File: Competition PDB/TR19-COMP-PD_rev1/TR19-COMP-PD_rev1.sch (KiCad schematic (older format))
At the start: 118 parts, among them J1 PWR BTN, J10 RGB_LED3, J11 Sen1, J12 Sen2, J13 Sen3, J14 Sen4, J15 BTN1, J16 BTN2, J17 BTN3, J18 BTN4, J19 BTN5, J2 PWR_LED, J20 BTN6, J21 BTN7, J22 BTN8, J23 BTN9, J24 Sen5, J25 Sen6, J26 Sen7, J27 Sen8, J28 BTN10, J29 BTN11, J3 PTT_LED, J30 BTN12, J31 BTN13, J32 BTN14, J33 BTN15, J34 BTN16, J35 LED1, J36 LED2, J37 LED3, J38 LED4, J39 LED5, J4 Servo1, J40 LED6, J41 LED7, J42 LED8, J43 LED9, J44 LED10, J45 LED11, J46 LED12, J47 LED13, J48 LED14, J49 LED15, J5 Servo2, J50 LED16, J6 Servo3, J7 BATT CONN, J8 RGB_LED1, J9 RGB_LED2, U1 SN74AHCT125_N_14, U2 SN74AHCT125_N_14, U3 SN74AHCT125_N_14, U4 SN74AHCT125_N_14

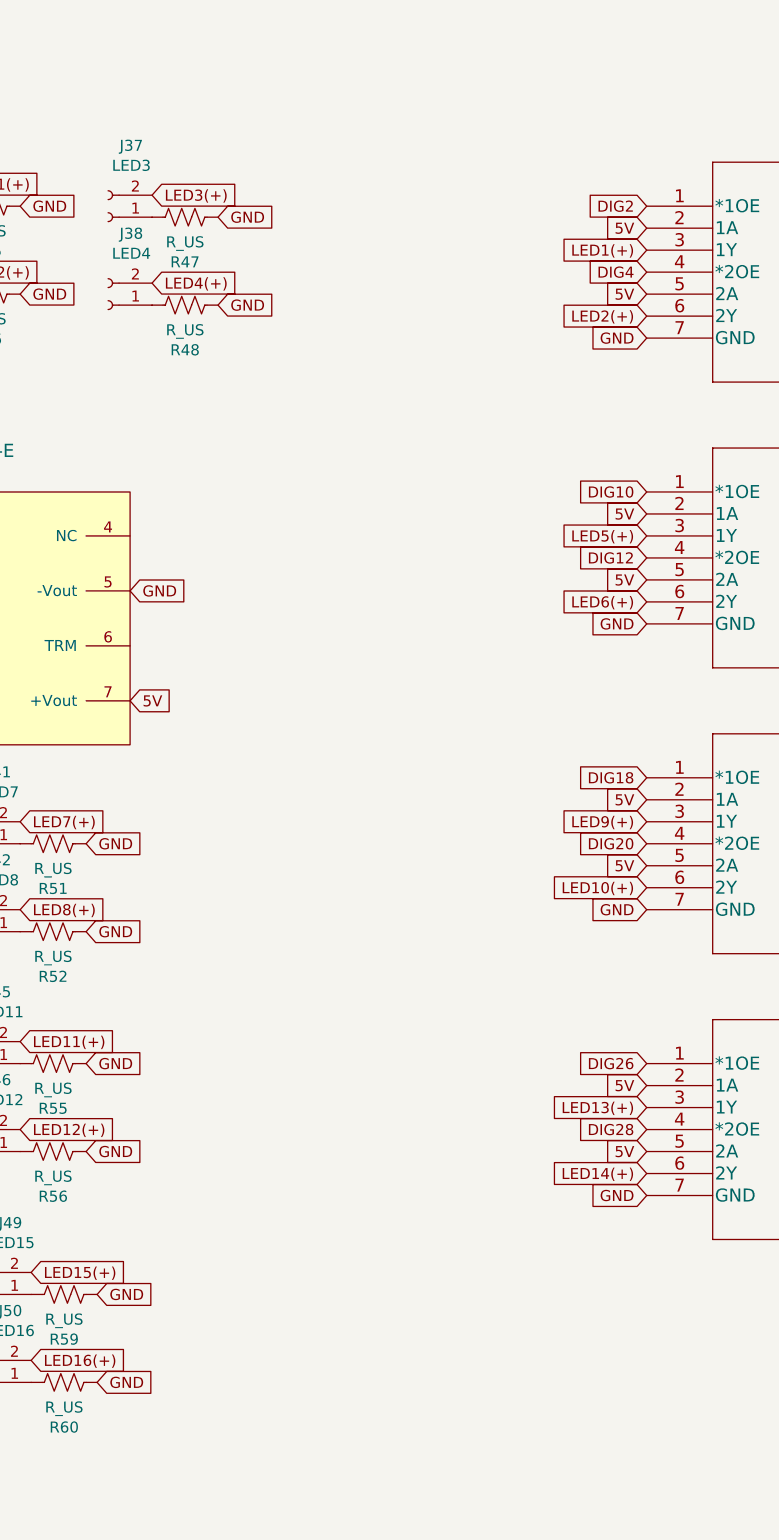
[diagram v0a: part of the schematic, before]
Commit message: Add pull up resistors for LED drivers
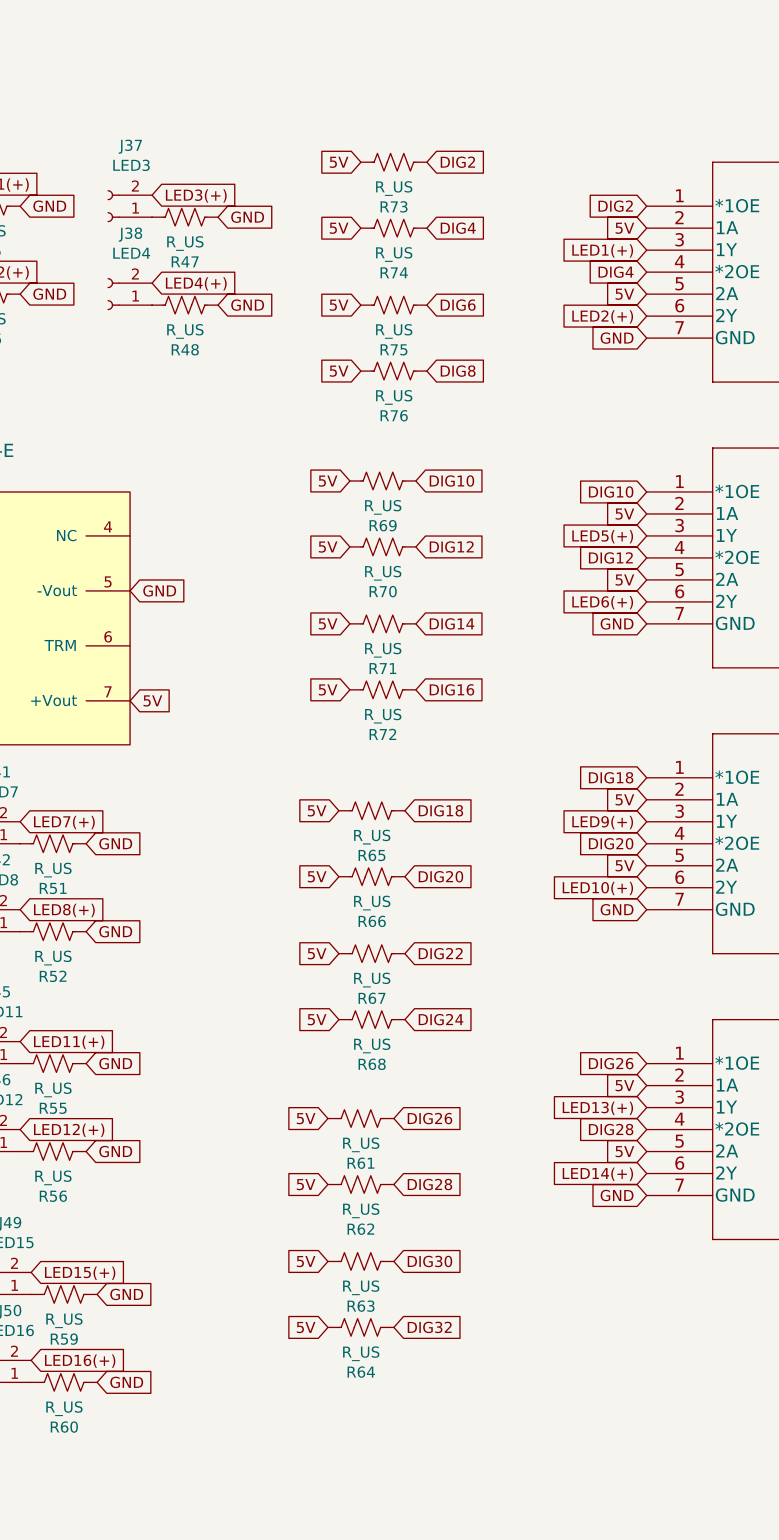
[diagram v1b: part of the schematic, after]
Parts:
- added R61, R62, R63, R64, R65, R66, R67, R68, R69, R70, R71, R72, R73, R74, R75, R76: R_US, Resistor_SMD:R_1210_3225Metric_Pad1.42x2.65mm_HandSolder, symbol Device:R_US
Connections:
- net 5V: now also R61.1, R62.1, R63.1, R64.1, R65.1, R66.1, R67.1, R68.1, R69.1, R70.1, R71.1, R72.1, R73.1, R74.1, R75.1, R76.1
- net DIG10: now also R69.2
- net DIG12: now also R70.2
- net DIG14: now also R71.2
- net DIG16: now also R72.2
- net DIG18: now also R65.2
- net DIG2: now also R73.2
- net DIG20: now also R66.2
- net DIG22: now also R67.2
- net DIG24: now also R68.2
- net DIG26: now also R61.2
- net DIG28: now also R62.2
- net DIG30: now also R63.2
- net DIG32: now also R64.2
- net DIG4: now also R74.2
- net DIG6: now also R75.2
- net DIG8: now also R76.2
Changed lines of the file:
@@
 Text GLabel 5850 6200 2    50   Input ~ 0
 GND
+$Comp
+L Device:R_US R73
+U 1 1 5CBA0F10
+P 7200 650
+F 0 "R73" V 6995 650 50  0000 C CNN
+F 1 "R_US" V 7086 650 50  0000 C CNN
+F 2 "Resistor_SMD:R_1210_3225Metric_Pad1.42x2.65mm_HandSolder" V 7240 640 50  0001 C CNN
+F 3 "~" H 7200 650 50  0001 C CNN
+	1    7200 650
+	0    -1   -1   0
+$EndComp
+Text GLabel 7350 650  2    50   Input ~ 0
+DIG2
+Text GLabel 7050 650  0    50   Input ~ 0
+5V
+$Comp
+L Device:R_US R74
+U 1 1 5CBA2910
+P 7200 950
+F 0 "R74" V 6995 950 50  0000 C CNN
+F 1 "R_US" V 7086 950 50  0000 C CNN
+F 2 "Resistor_SMD:R_1210_3225Metric_Pad1.42x2.65mm_HandSolder" V 7240 940 50  0001 C CNN
+F 3 "~" H 7200 950 50  0001 C CNN
+	1    7200 950
+	0    -1   -1   0
+$EndComp
+Text GLabel 7350 950  2    50   Input ~ 0
+DIG4
+Text GLabel 7050 950  0    50   Input ~ 0
+5V
+$Comp
+L Device:R_US R75
+U 1 1 5CBA344B
+P 7200 1300
+F 0 "R75" V 6995 1300 50  0000 C CNN
+F 1 "R_US" V 7086 1300 50  0000 C CNN
+F 2 "Resistor_SMD:R_1210_3225Metric_Pad1.42x2.65mm_HandSolder" V 7240 1290 50  0001 C CNN
+F 3 "~" H 7200 1300 50  0001 C CNN
+	1    7200 1300
+	0    -1   -1   0
+$EndComp
+Text GLabel 7350 1300 2    50   Input ~ 0
+DIG6
+Text GLabel 7050 1300 0    50   Input ~ 0
+5V
+$Comp
+L Device:R_US R76
+U 1 1 5CBA3454
+P 7200 1600
+F 0 "R76" V 6995 1600 50  0000 C CNN
+F 1 "R_US" V 7086 1600 50  0000 C CNN
+F 2 "Resistor_SMD:R_1210_3225Metric_Pad1.42x2.65mm_HandSolder" V 7240 1590 50  0001 C CNN
+F 3 "~" H 7200 1600 50  0001 C CNN
+	1    7200 1600
+	0    -1   -1   0
+$EndComp
+Text GLabel 7350 1600 2    50   Input ~ 0
+DIG8
+Text GLabel 7050 1600 0    50   Input ~ 0
+5V
+$Comp
+L Device:R_US R69
+U 1 1 5CBA3E70
+P 7150 2100
+F 0 "R69" V 6945 2100 50  0000 C CNN
+F 1 "R_US" V 7036 2100 50  0000 C CNN
+F 2 "Resistor_SMD:R_1210_3225Metric_Pad1.42x2.65mm_HandSolder" V 7190 2090 50  0001 C CNN
+F 3 "~" H 7150 2100 50  0001 C CNN
+	1    7150 2100
+	0    -1   -1   0
+$EndComp
+Text GLabel 7300 2100 2    50   Input ~ 0
+DIG10
+Text GLabel 7000 2100 0    50   Input ~ 0
+5V
+$Comp
+L Device:R_US R70
+U 1 1 5CBA3E79
+P 7150 2400
+F 0 "R70" V 6945 2400 50  0000 C CNN
+F 1 "R_US" V 7036 2400 50  0000 C CNN
+F 2 "Resistor_SMD:R_1210_3225Metric_Pad1.42x2.65mm_HandSolder" V 7190 2390 50  0001 C CNN
+F 3 "~" H 7150 2400 50  0001 C CNN
+	1    7150 2400
+	0    -1   -1   0
+$EndComp
+Text GLabel 7300 2400 2    50   Input ~ 0
+DIG12
+Text GLabel 7000 2400 0    50   Input ~ 0
+5V
+$Comp
+L Device:R_US R71
+U 1 1 5CBA3E82
+P 7150 2750
+F 0 "R71" V 6945 2750 50  0000 C CNN
+F 1 "R_US" V 7036 2750 50  0000 C CNN
+F 2 "Resistor_SMD:R_1210_3225Metric_Pad1.42x2.65mm_HandSolder" V 7190 2740 50  0001 C CNN
+F 3 "~" H 7150 2750 50  0001 C CNN
+	1    7150 2750
+	0    -1   -1   0
+$EndComp
+Text GLabel 7300 2750 2    50   Input ~ 0
+DIG14
+Text GLabel 7000 2750 0    50   Input ~ 0
+5V
+$Comp
+L Device:R_US R72
+U 1 1 5CBA3E8B
+P 7150 3050
+F 0 "R72" V 6945 3050 50  0000 C CNN
+F 1 "R_US" V 7036 3050 50  0000 C CNN
+F 2 "Resistor_SMD:R_1210_3225Metric_Pad1.42x2.65mm_HandSolder" V 7190 3040 50  0001 C CNN
+F 3 "~" H 7150 3050 50  0001 C CNN
+	1    7150 3050
+	0    -1   -1   0
+$EndComp
+Text GLabel 7300 3050 2    50   Input ~ 0
+DIG16
+Text GLabel 7000 3050 0    50   Input ~ 0
+5V
+$Comp
+L Device:R_US R65
+U 1 1 5CBA4161
+P 7100 3600
+F 0 "R65" V 6895 3600 50  0000 C CNN
+F 1 "R_US" V 6986 3600 50  0000 C CNN
+F 2 "Resistor_SMD:R_1210_3225Metric_Pad1.42x2.65mm_HandSolder" V 7140 3590 50  0001 C CNN
+F 3 "~" H 7100 3600 50  0001 C CNN
+	1    7100 3600
+	0    -1   -1   0
+$EndComp
+Text GLabel 7250 3600 2    50   Input ~ 0
+DIG18
+Text GLabel 6950 3600 0    50   Input ~ 0
+5V
+$Comp
+L Device:R_US R66
+U 1 1 5CBA416A
+P 7100 3900
+F 0 "R66" V 6895 3900 50  0000 C CNN
+F 1 "R_US" V 6986 3900 50  0000 C CNN
+F 2 "Resistor_SMD:R_1210_3225Metric_Pad1.42x2.65mm_HandSolder" V 7140 3890 50  0001 C CNN
+F 3 "~" H 7100 3900 50  0001 C CNN
+	1    7100 3900
+	0    -1   -1   0
+$EndComp
+Text GLabel 7250 3900 2    50   Input ~ 0
+DIG20
+Text GLabel 6950 3900 0    50   Input ~ 0
+5V
+$Comp
+L Device:R_US R67
+U 1 1 5CBA4173
+P 7100 4250
+F 0 "R67" V 6895 4250 50  0000 C CNN
+F 1 "R_US" V 6986 4250 50  0000 C CNN
+F 2 "Resistor_SMD:R_1210_3225Metric_Pad1.42x2.65mm_HandSolder" V 7140 4240 50  0001 C CNN
+F 3 "~" H 7100 4250 50  0001 C CNN
+	1    7100 4250
+	0    -1   -1   0
+$EndComp
+Text GLabel 7250 4250 2    50   Input ~ 0
+DIG22
+Text GLabel 6950 4250 0    50   Input ~ 0
+5V
+$Comp
+L Device:R_US R68
+U 1 1 5CBA417C
+P 7100 4550
+F 0 "R68" V 6895 4550 50  0000 C CNN
+F 1 "R_US" V 6986 4550 50  0000 C CNN
+F 2 "Resistor_SMD:R_1210_3225Metric_Pad1.42x2.65mm_HandSolder" V 7140 4540 50  0001 C CNN
+F 3 "~" H 7100 4550 50  0001 C CNN
+	1    7100 4550
+	0    -1   -1   0
+$EndComp
+Text GLabel 7250 4550 2    50   Input ~ 0
+DIG24
+Text GLabel 6950 4550 0    50   Input ~ 0
+5V
+$Comp
+L Device:R_US R61
+U 1 1 5CBA4813
+P 7050 5000
+F 0 "R61" V 6845 5000 50  0000 C CNN
+F 1 "R_US" V 6936 5000 50  0000 C CNN
+F 2 "Resistor_SMD:R_1210_3225Metric_Pad1.42x2.65mm_HandSolder" V 7090 4990 50  0001 C CNN
+F 3 "~" H 7050 5000 50  0001 C CNN
+	1    7050 5000
+	0    -1   -1   0
+$EndComp
+Text GLabel 7200 5000 2    50   Input ~ 0
+DIG26
+Text GLabel 6900 5000 0    50   Input ~ 0
+5V
+$Comp
+L Device:R_US R62
+U 1 1 5CBA481C
+P 7050 5300
+F 0 "R62" V 6845 5300 50  0000 C CNN
+F 1 "R_US" V 6936 5300 50  0000 C CNN
+F 2 "Resistor_SMD:R_1210_3225Metric_Pad1.42x2.65mm_HandSolder" V 7090 5290 50  0001 C CNN
+F 3 "~" H 7050 5300 50  0001 C CNN
+	1    7050 5300
+	0    -1   -1   0
+$EndComp
+Text GLabel 7200 5300 2    50   Input ~ 0
+DIG28
+Text GLabel 6900 5300 0    50   Input ~ 0
+5V
+$Comp
+L Device:R_US R63
+U 1 1 5CBA4825
+P 7050 5650
+F 0 "R63" V 6845 5650 50  0000 C CNN
+F 1 "R_US" V 6936 5650 50  0000 C CNN
+F 2 "Resistor_SMD:R_1210_3225Metric_Pad1.42x2.65mm_HandSolder" V 7090 5640 50  0001 C CNN
+F 3 "~" H 7050 5650 50  0001 C CNN
+	1    7050 5650
+	0    -1   -1   0
+$EndComp
+Text GLabel 7200 5650 2    50   Input ~ 0
+DIG30
+Text GLabel 6900 5650 0    50   Input ~ 0
+5V
+$Comp
+L Device:R_US R64
+U 1 1 5CBA482E
+P 7050 5950
+F 0 "R64" V 6845 5950 50  0000 C CNN
+F 1 "R_US" V 6936 5950 50  0000 C CNN
+F 2 "Resistor_SMD:R_1210_3225Metric_Pad1.42x2.65mm_HandSolder" V 7090 5940 50  0001 C CNN
+F 3 "~" H 7050 5950 50  0001 C CNN
+	1    7050 5950
+	0    -1   -1   0
+$EndComp
+Text GLabel 7200 5950 2    50   Input ~ 0
+DIG32
+Text GLabel 6900 5950 0    50   Input ~ 0
+5V
 $EndSCHEMATC
